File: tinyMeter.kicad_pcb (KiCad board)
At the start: 2 copper layers, 74.6 x 70 mm, 84 parts, among them J1 USB_MASTER, J2 DC_POWER, J3 USB_POWER, J4 USBA_OUT_2, J5 USBA_OUT_1, J6 DC_POWER, Q1 BUK9832-55A, Q2 BUK9832-55A, Q3 BUK9832-55A, Q4 SS8050, SW1 SW_Push, SW2 SW_Push, SW3 SW_Push, SW4 SW_Push, SW5 SW_Push, SW6 SW_Push, SW7 SW_Push, U1 ESP32-S3, U2 INA219AxD, U3 INA219AxD, U4 INA219AxD, U5 AMS1117-3.3, Y1 40M

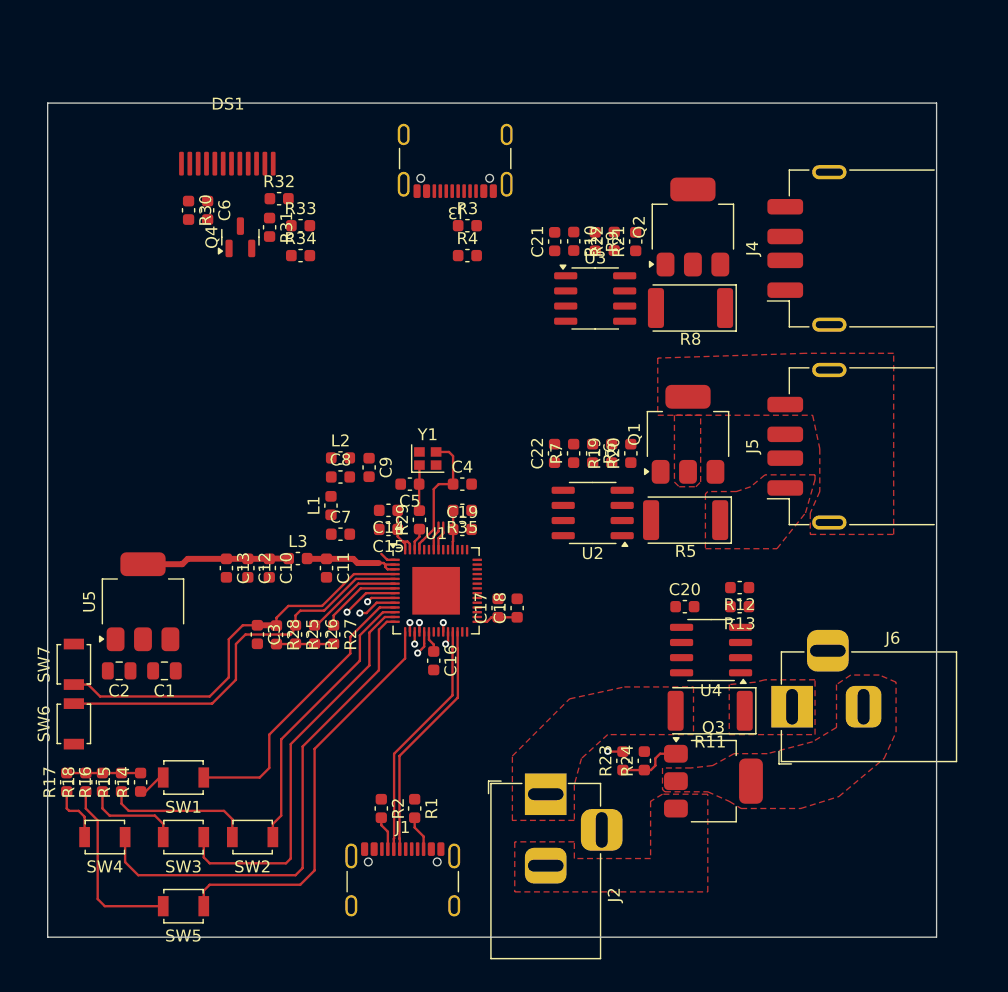
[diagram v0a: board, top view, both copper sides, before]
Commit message: Rough layout and routing
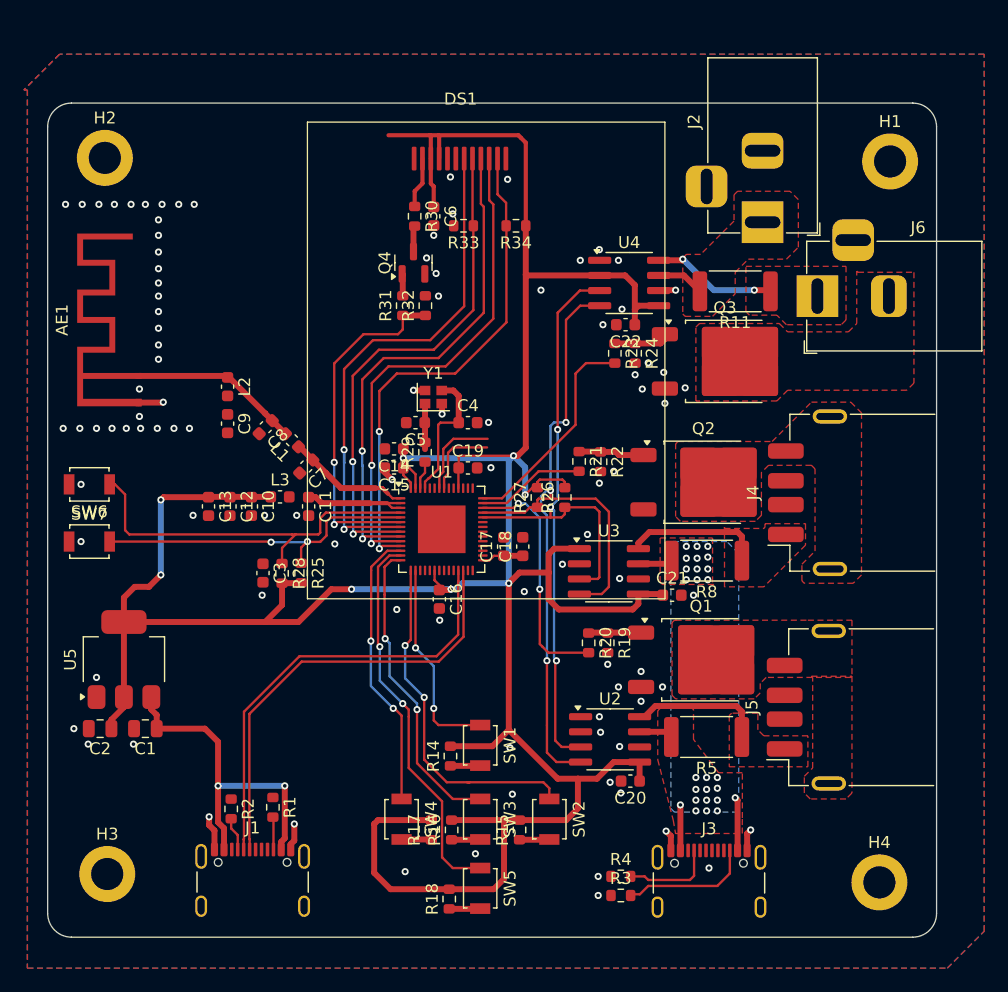
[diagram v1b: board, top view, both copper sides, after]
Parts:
- removed R10, R12, R13, R6, R7, R9: 0R, Capacitor_SMD:C_0603_1608Metric
- removed R35: 10k, Capacitor_SMD:C_0603_1608Metric
- added AE1: Antenna_Loop, Library:ESPRESSIF_ESP32_MIFA_2.4GHz_Right, F.Cu at (146.6, 97.2)
- added H1: 1, MountingHole:MountingHole_2.7mm_M2.5_DIN965_Pad, F.Cu at (209.7, 79.3)
- added H2: 2, MountingHole:MountingHole_2.7mm_M2.5_DIN965_Pad, F.Cu at (143.8, 79.0)
- added H3: 3, MountingHole:MountingHole_2.7mm_M2.5_DIN965_Pad, F.Cu at (144.0, 139.1)
- added H4: 4, MountingHole:MountingHole_2.7mm_M2.5_DIN965_Pad, F.Cu at (208.8, 139.8)
- Q1, Q2, Q3: value BUK9832-55A -> 100N03A; footprint Package_TO_SOT_SMD:SOT-223-3_TabPin2 -> Package_TO_SOT_SMD:TO-252-2
- R1, R14, R15, R16, R17, R18, R19, R2, R20, R21, R22, R23, R24, R25, R26, R27, R28, R29, R3, R30, R31, R32, R33, R34, R4: footprint Capacitor_SMD:C_0603_1608Metric -> Resistor_SMD:R_0603_1608Metric
- R11, R5, R8: footprint Diode_SMD:D_2512_6332Metric -> Resistor_SMD:R_2512_6332Metric
- moved J3 66.2 mm to (194.5, 140.8), turned to 0 degrees
- moved R3 57.7 mm to (187.1, 140.9)
- moved R4 53.7 mm to (187.1, 139.3)
- moved J2 51.3 mm to (199.0, 84.4), turned to -90 degrees
- moved R11 35.3 mm to (196.7, 90.2)
- moved Q3 35.2 mm to (195.8, 96.1)
- moved J6 34.5 mm to (203.6, 90.6)
- moved R24 34.2 mm to (188.3, 95.4), turned to -90 degrees
- moved R23 34.2 mm to (186.6, 95.4), turned to -90 degrees
- moved R15 33.6 mm to (178.6, 135.4)
- moved R18 32.0 mm to (172.7, 141.2)
- moved U4 31.6 mm to (187.8, 89.5), turned to 0 degrees
- moved C21 31.3 mm to (191.4, 115.7), turned to 0 degrees
- moved R17 30.9 mm to (171.2, 135.4)
- moved R16 29.6 mm to (172.9, 135.4)
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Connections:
- net Net-(J4-GND) renamed /USBA_OUT2_GND
- J4 pad 1: Net-(J4-VBUS) -> /USBA_OUT2_VCC
- R8 pad 1: Net-(J4-VBUS) -> /USBA_OUT2_VCC
- U1 pad 10: /DC_POWER_FETGATE -> /DISPLAY_SDA
- U1 pad 11: /KEYPAD_K1 -> /DISPLAY_RST
- U1 pad 12: /KEYPAD_K2 -> /KEYPAD_K4
- U1 pad 13: /KEYPAD_K3 -> /KEYPAD_K5
- U1 pad 14: /KEYPAD_K4 -> /KEYPAD_K3
- U1 pad 15: /KEYPAD_K5 -> /KEYPAD_K2
- U1 pad 16: /DISPLAY_DC -> /KEYPAD_K1
- U1 pad 17: /DISPLAY_CS -> unconnected-(U1-GPIO12-Pad17)
- U1 pad 18: /DISPLAY_SCK -> unconnected-(U1-GPIO13-Pad18)
- U1 pad 19: /DISPLAY_SDA -> unconnected-(U1-GPIO14-Pad19)
- U1 pad 23: /DISPLAY_RST -> unconnected-(U1-GPIO17-Pad23)
- U1 pad 24: /DISPLAY_BLK -> unconnected-(U1-GPIO18-Pad24)
- U1 pad 38: unconnected-(U1-GPIO33-Pad38) -> /METER_SDA
- U1 pad 39: unconnected-(U1-GPIO34-Pad39) -> /METER_SCL
- U1 pad 40: unconnected-(U1-GPIO35-Pad40) -> /USBA_OUT_1_FETGATE
- U1 pad 41: unconnected-(U1-GPIO36-Pad41) -> /USBA_OUT_2_FETGATE
- U1 pad 42: unconnected-(U1-GPIO37-Pad42) -> /DC_POWER_FETGATE
- U1 pad 6: /METER_SDA -> /DISPLAY_BLK
- U1 pad 7: /METER_SCL -> /DISPLAY_DC
- U1 pad 8: /USBA_OUT_1_FETGATE -> /DISPLAY_CS
- U1 pad 9: /USBA_OUT_2_FETGATE -> /DISPLAY_SCK
- U2 pad 1: Net-(U2-A1) -> GND
- U2 pad 2: Net-(U2-A0) -> GND
- U2 pad 7: /USBA_OUT1_VCC -> PWR_5V
- U2 pad 8: PWR_5V -> /USBA_OUT1_VCC
- U3 pad 1: Net-(U3-A1) -> +3V3
- U3 pad 2: Net-(U3-A0) -> GND
- U3 pad 7: Net-(J4-VBUS) -> PWR_5V
- U3 pad 8: PWR_5V -> /USBA_OUT2_VCC
- U4 pad 1: Net-(U4-A1) -> GND
- U4 pad 2: Net-(U4-A0) -> +3V3
- U4 pad 7: /DC_POWER_VCC -> PWR_DC
- U4 pad 8: PWR_DC -> /DC_POWER_VCC
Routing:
- net +3V3: track 33.3 -> 269.7 mm, vias 0 -> 8
- net /METER_SCL: track 6.92 -> 66.2 mm, vias 0 -> 3
- net /METER_SDA: track 8.20 -> 61.8 mm, vias 0 -> 3
- net /DISPLAY_DC: track 0.78 -> 44.0 mm, vias 1 -> 2
- net /DISPLAY_RST: track 0.78 -> 42.3 mm, vias 1 -> 2
- net /DISPLAY_CS: track 1.02 -> 42.5 mm, vias 1 -> 2
- net /DISPLAY_SCK: track 0.78 -> 42.2 mm, vias 1 -> 2
- net /DISPLAY_SDA: track 2.01 -> 42.1 mm, vias 1 -> 2
- net USB_VBUS: track 0.00 -> 28.8 mm, vias 0 -> 2
- net /DISPLAY_BLK: track 1.10 -> 29.2 mm, vias 1 -> 2
- net /KEYPAD_K4: track 42.0 -> 23.6 mm, vias 0 -> 2
- net /USB_MASTER_D+: track 20.3 -> 37.6 mm
- net /USB_MASTER_D-: track 20.3 -> 37.6 mm
- net /USBA_OUT_1_FETGATE: track 4.69 -> 20.4 mm, vias 1 -> 2
- net GND: track 0.00 -> 15.5 mm, vias 0 -> 67
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- added copper zone on F.Cu, net /USBA_OUT2_GND
- added copper zone on F.Cu, net /USBA_OUT2_VCC
- added copper zone on B.Cu, net GND
- added copper zone on B.Cu, net PWR_5V
- added copper zone on F.Cu, net PWR_5V
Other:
- outline, holes or cut-outs redrawn

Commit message: More layout
- Some traces refactor
- Add debug connector with UART lines
- Add external WiFi/BT connector and selector for PCB/Ext
- Add WS8212B LED just for fun
- Add power indication LED on 3V3
- Remove RefDes silkscreen; add useful silkscreen
- Add crystal 3D model
- Move display FPC connector to back side of the PCB; reroute display traces
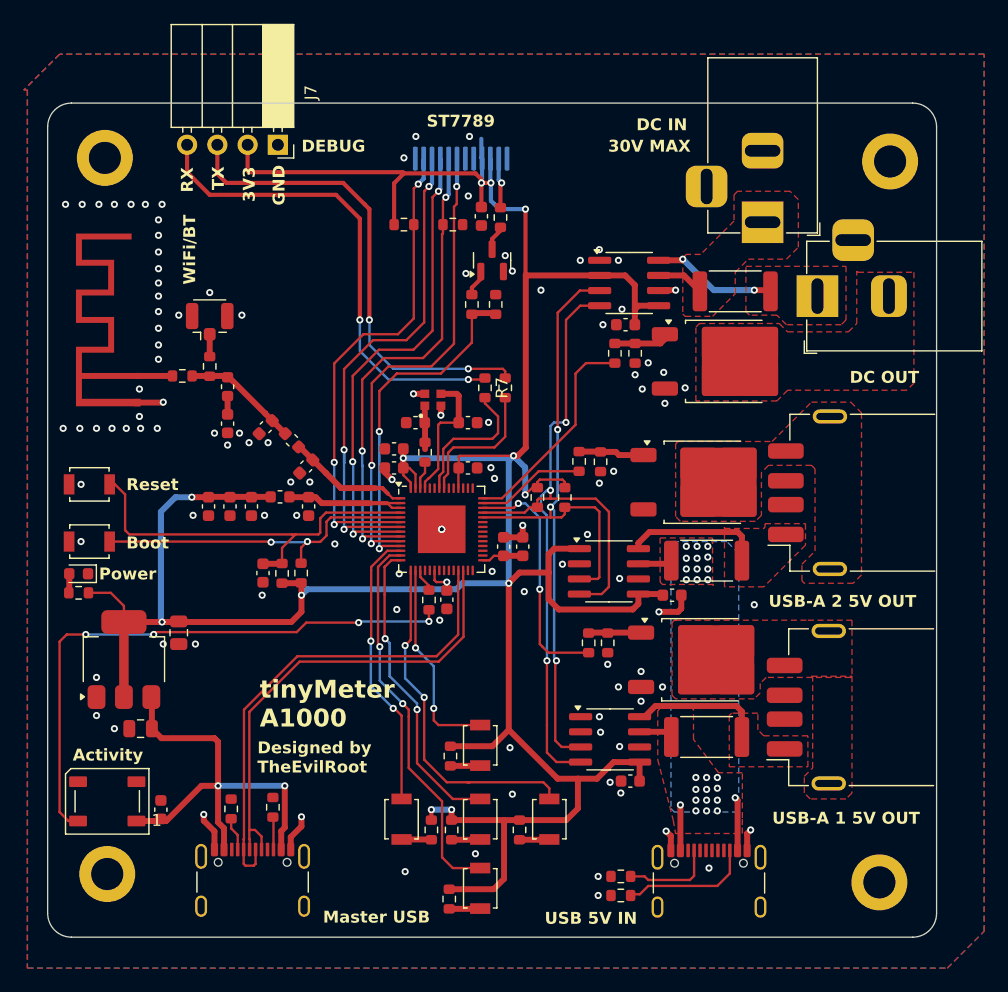
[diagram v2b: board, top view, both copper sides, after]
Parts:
- added C23: 100n, Capacitor_SMD:C_0603_1608Metric, F.Cu at (148.5, 133.7)
- added D1: WS2812B, LED_SMD:LED_WS2812B_PLCC4_5.0x5.0mm_P3.2mm, F.Cu at (144.0, 133.0)
- added D2: PWR_LED, LED_SMD:LED_0603_1608Metric, F.Cu at (141.6, 113.9)
- added J7: Debug, Connector_PinSocket_2.54mm:PinSocket_1x04_P2.54mm_Horizontal, F.Cu at (158.3, 77.9)
- added J8: External antenna, Connector_Coaxial:U.FL_Hirose_U.FL-R-SMT-1_Vertical, F.Cu at (152.6, 92.8)
- added R10: 0R, Resistor_SMD:R_0603_1608Metric, F.Cu at (152.6, 96.5)
- added R12: 220, Resistor_SMD:R_0603_1608Metric, F.Cu at (171.0, 116.1)
- added R13: 220, Resistor_SMD:R_0603_1608Metric, F.Cu at (141.6, 115.5)
- added R6: 0R, Resistor_SMD:R_0603_1608Metric, F.Cu at (177.4, 98.3)
- added R7: 0R, Resistor_SMD:R_0603_1608Metric, F.Cu at (175.7, 98.3)
- added R9: 0R, Resistor_SMD:R_0603_1608Metric, F.Cu at (150.3, 97.3)
- AE1: value Antenna_Loop -> PCB antenna
- DS1: moved to B.Cu
- L1, L2, L3: footprint Capacitor_SMD:C_0603_1608Metric -> Inductor_SMD:L_0603_1608Metric
- Y1: value 40M -> Crystal_GND24; footprint Crystal:Crystal_SMD_2016-4Pin_2.0x1.6mm -> Library:OSC_XRCGB40M000F4M00R0
- moved C2 10.4 mm to (150.0, 118.8), turned to -90 degrees
- moved R34 9.40 mm to (168.9, 84.6), turned to 0 degrees
- moved R30 7.20 mm to (177.0, 84.0)
- moved Q4 6.60 mm to (176.3, 87.6)
- moved R32 5.90 mm to (176.6, 91.3)
- moved R31 5.80 mm to (174.6, 91.3)
- moved C6 4.00 mm to (175.4, 83.9)
- moved R33 0.91 mm to (173.0, 84.6), turned to 0 degrees
- moved C16 0.63 mm to (172.5, 116.1)
- moved C1 0.40 mm to (146.8, 126.9)
- moved Y1 0.23 mm to (171.3, 99.3), turned to 90 degrees
- moved AE1 0.10 mm to (146.5, 97.2)
- turned DS1 to 180 degrees
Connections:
- AE1 pad 1: /WIFI_ANTENNA -> Net-(AE1-Pad1)
- U1 pad 10: /DISPLAY_SDA -> /DISPLAY_DC
- U1 pad 11: /DISPLAY_RST -> /DISPLAY_BLK
- U1 pad 17: unconnected-(U1-GPIO12-Pad17) -> /MCU_LED_DATA
- U1 pad 49: /ESP_TX -> Net-(U1-U0TXD)
- U1 pad 50: /ESP_RX -> Net-(U1-U0RXD)
- U1 pad 6: /DISPLAY_BLK -> /DISPLAY_RST
- U1 pad 7: /DISPLAY_DC -> /DISPLAY_SDA
- U1 pad 8: /DISPLAY_CS -> /DISPLAY_SCK
- U1 pad 9: /DISPLAY_SCK -> /DISPLAY_CS
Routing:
- net Net-(D1-DIN): track 0.00 -> 48.8 mm, vias 0 -> 4
- net /ESP_TX: track 6.57 -> 40.7 mm, vias 0 -> 2
- net /ESP_RX: track 7.51 -> 41.1 mm, vias 0 -> 2
- net Net-(U1-U0RXD): track 0.00 -> 12.0 mm
- net Net-(U1-U0TXD): track 0.00 -> 11.7 mm
- net USB_VBUS: track 28.8 -> 37.1 mm
- net GND: track 15.5 -> 22.3 mm, vias 67 -> 85
- net /WIFI_ANTENNA: track 14.5 -> 9.93 mm
- net /DISPLAY_DC: track 44.0 -> 39.9 mm, vias 2 -> 3
- net /USB_MASTER_D-: track 37.6 -> 41.3 mm
- net Net-(AE1-Pad1): track 0.00 -> 3.04 mm
- net /USB_MASTER_D+: track 37.6 -> 40.1 mm
- net /DISPLAY_CS: track 42.5 -> 40.1 mm, vias 2 -> 3
- net /MCU_LED_DATA: track 0.00 -> 1.96 mm
- net /DISPLAY_SCK: track 42.2 -> 40.3 mm, vias 2 -> 3
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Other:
- board text added: "30V MAX"
- board text added: "3V3"
- board text added: "Activity"
- board text added: "Boot"
- board text added: "DC IN"
- board text added: "DC OUT"
- board text added: "DEBUG"
- board text added: "Designed by TheEvilRoot"
- board text added: "GND"
- board text added: "Master USB"
- board text added: "Power"
- board text added: "RX"
- board text added: "Reset"
- board text added: "ST7789"
- board text added: "TX"
- board text added: "USB 5V IN"
- board text added: "USB-A 1 5V OUT"
- board text added: "USB-A 2 5V OUT"
- board text added: "WiFi/BT"
- board text added: "tinyMeter A1000"

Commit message: Fixes and schematic refactor
- Refactor schematic to get more space
- Assign nets where missing
- Change footprint of USB-C
- Add 3D model for USB-C footprint
- Changes to board setup
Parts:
- J1, J3: footprint Connector_USB:USB_C_Receptacle_GCT_USB4105-xx-A_16P_TopMnt_Horizontal -> Connector_USB:USB_C_Receptacle_HRO_TYPE-C-31-M-12
- SW6: value SW_Push -> Boot
- SW7: value SW_Push -> Reset
- moved C4 0.37 mm to (173.9, 101.2)
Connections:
- net Net-(AE1-Pad1) renamed /WIFI_ANTENNA_PCB
- net Net-(C9-Pad1) renamed /WIFI_ANTENNA_F
- net Net-(D1-DIN) renamed /MCU_LED_DIN
- net Net-(D2-Pad2) renamed /3V3_PWR_LED
- net Net-(DS1-LEDK) renamed /DISPLAY_LEDK
- net Net-(J1-CC1) renamed /USB_MASTER_CC1
- net Net-(J1-CC2) renamed /USB_MASTER_CC2
- net Net-(J3-CC1) renamed /USB_POWER_CC1
- net Net-(J3-CC2) renamed /USB_POWER_CC2
- net Net-(J8-In) renamed /WIFI_ANTENNA_EXT
- net Net-(Q2-G) renamed /USBA_OUT2_GATE
- net Net-(Q3-G) renamed /DC_POWER_GATE
- net Net-(Q4-B) renamed /DISPLAY_BLK_GATE
- net Net-(Q4-C) renamed /DISPLAY_LEDK_R
- net Net-(U1-U0RXD) renamed /ESP_RDX0
- net Net-(U1-U0TXD) renamed /ESP_TDX0
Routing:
- net PWR_5V: track 14.0 -> 12.7 mm
- net /ESP_XTAL_N: track 11.4 -> 10.2 mm
- net /ESP_XTAL_IN: track 3.69 -> 3.12 mm
- net GND: track 22.3 -> 21.8 mm, vias 85 -> 97

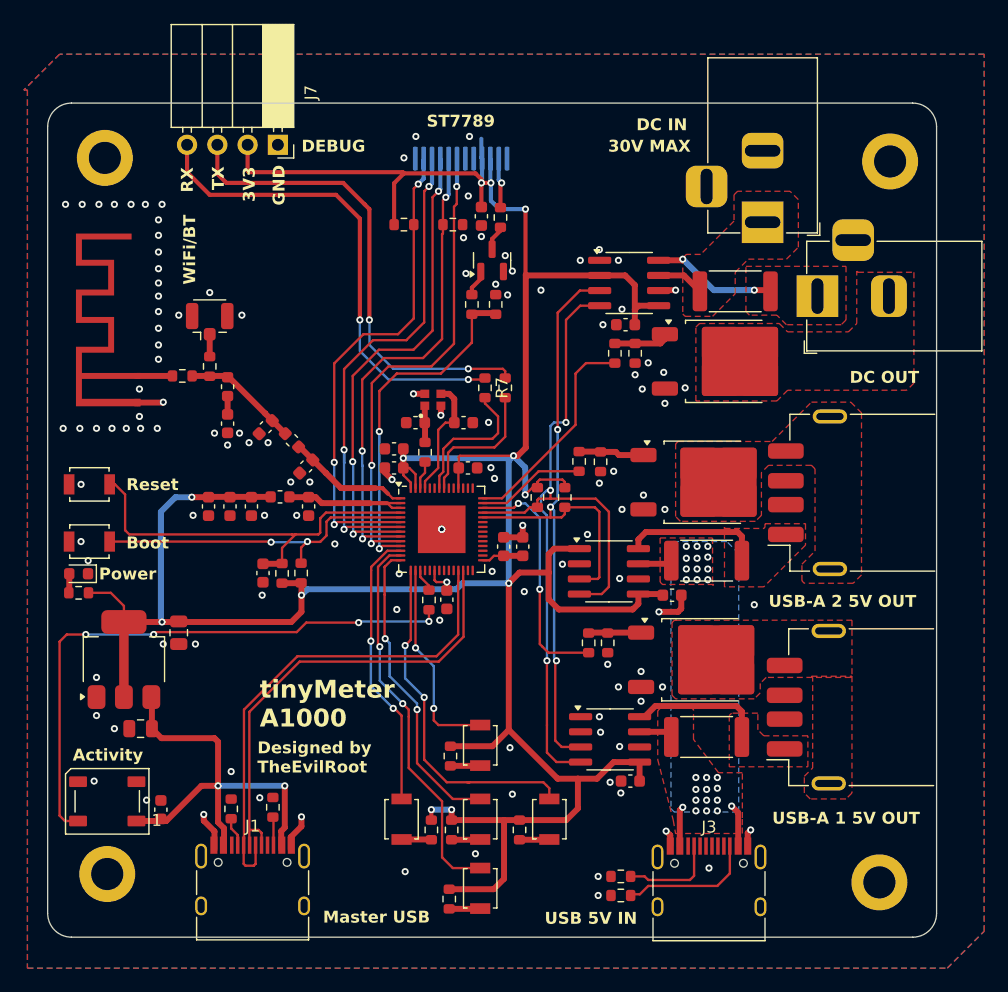
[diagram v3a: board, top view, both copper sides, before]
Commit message: Some rerouting. Via stitching. Align mouting holes
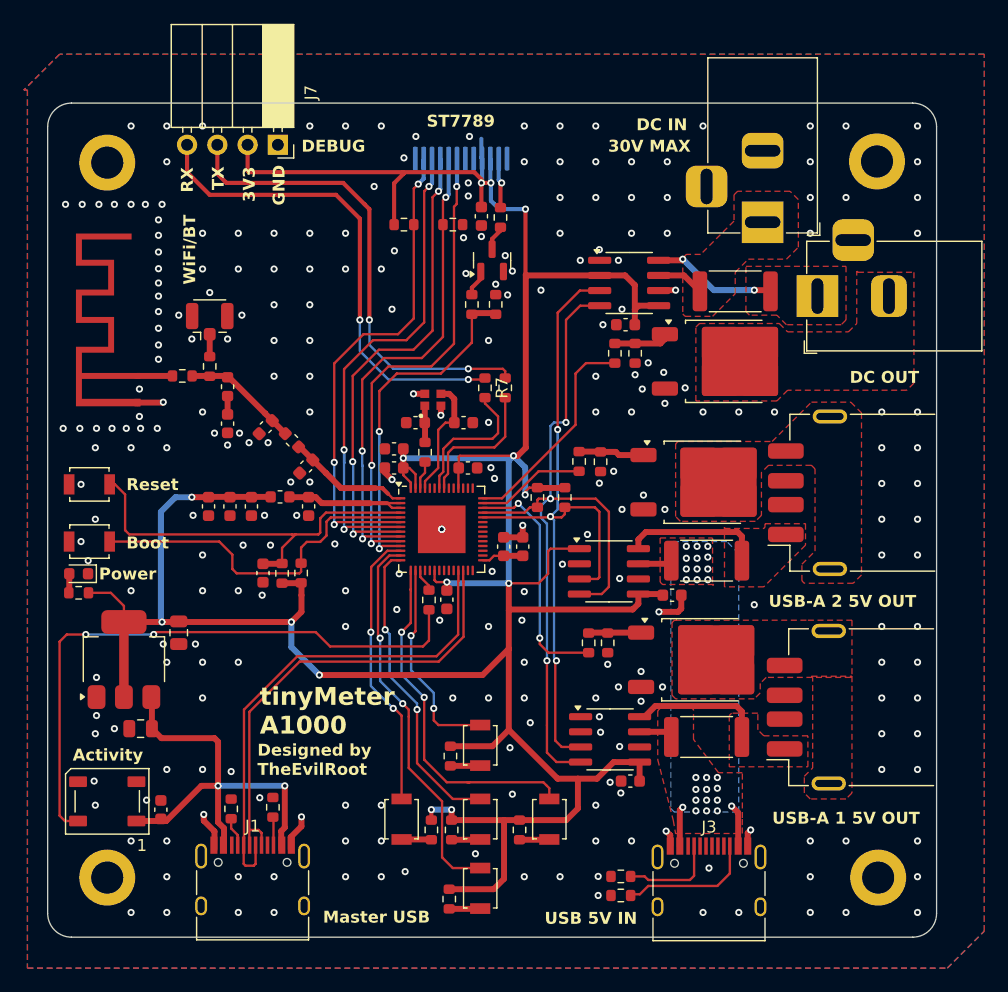
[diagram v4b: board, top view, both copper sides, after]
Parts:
- moved H1 1.10 mm to (208.6, 79.3)
- moved H2 0.45 mm to (144.0, 79.4)
- moved H4 0.41 mm to (208.7, 139.4)
- moved H3 0.30 mm to (144.0, 139.4)
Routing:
- net +3V3: track 270.1 -> 278.8 mm, vias 13 -> 14
- net /ESP_IO0: track 28.1 -> 30.1 mm, vias 2 -> 0
- net /MCU_LED_DIN: track 49.0 -> 50.9 mm, vias 4 -> 2
- net /METER_SDA: track 61.8 -> 61.0 mm
- net /METER_SCL: track 66.2 -> 65.5 mm
- net GND: vias 97 -> 240
